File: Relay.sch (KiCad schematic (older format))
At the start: 0 parts

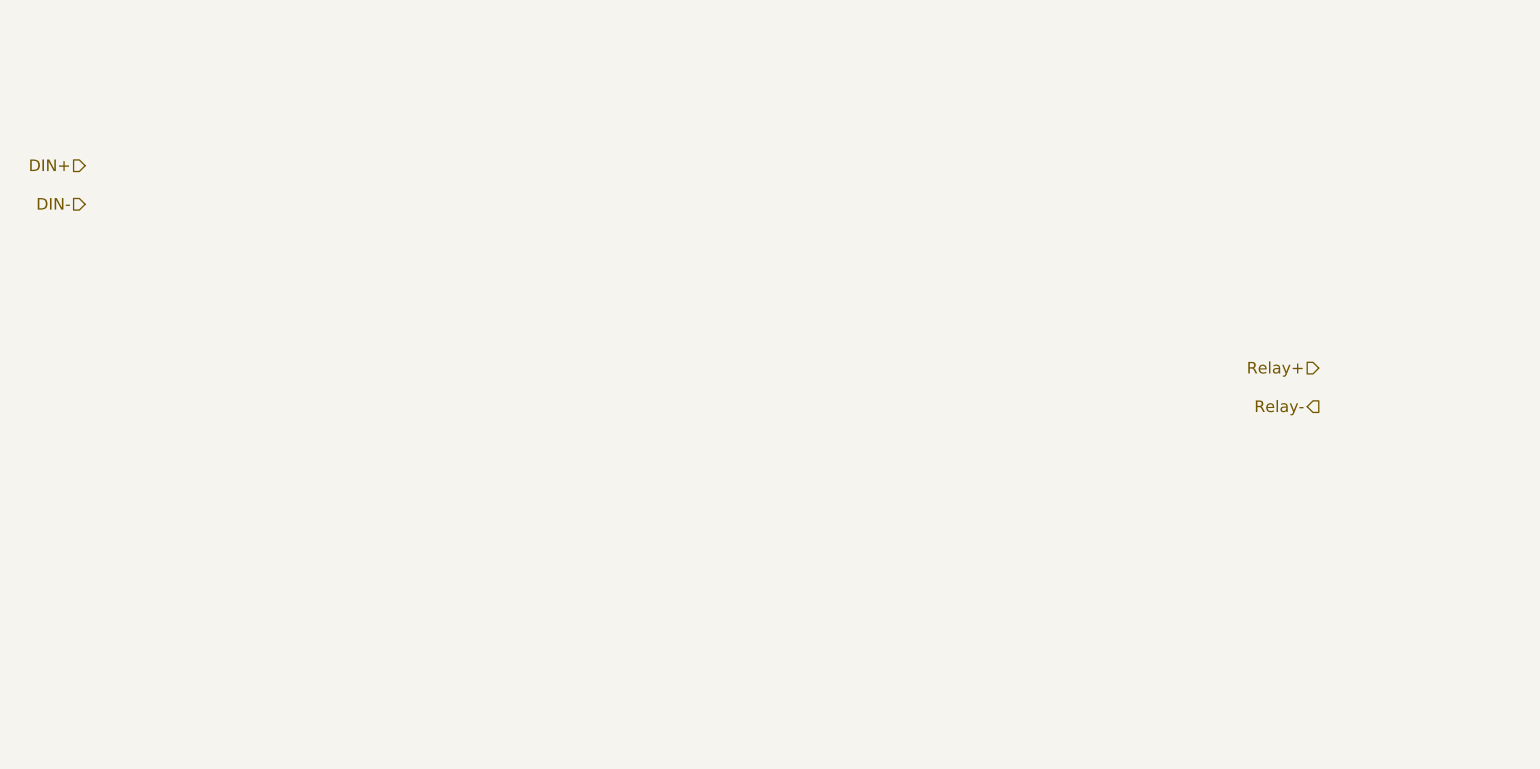
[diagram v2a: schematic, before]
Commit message: Added Relay Module Schematic
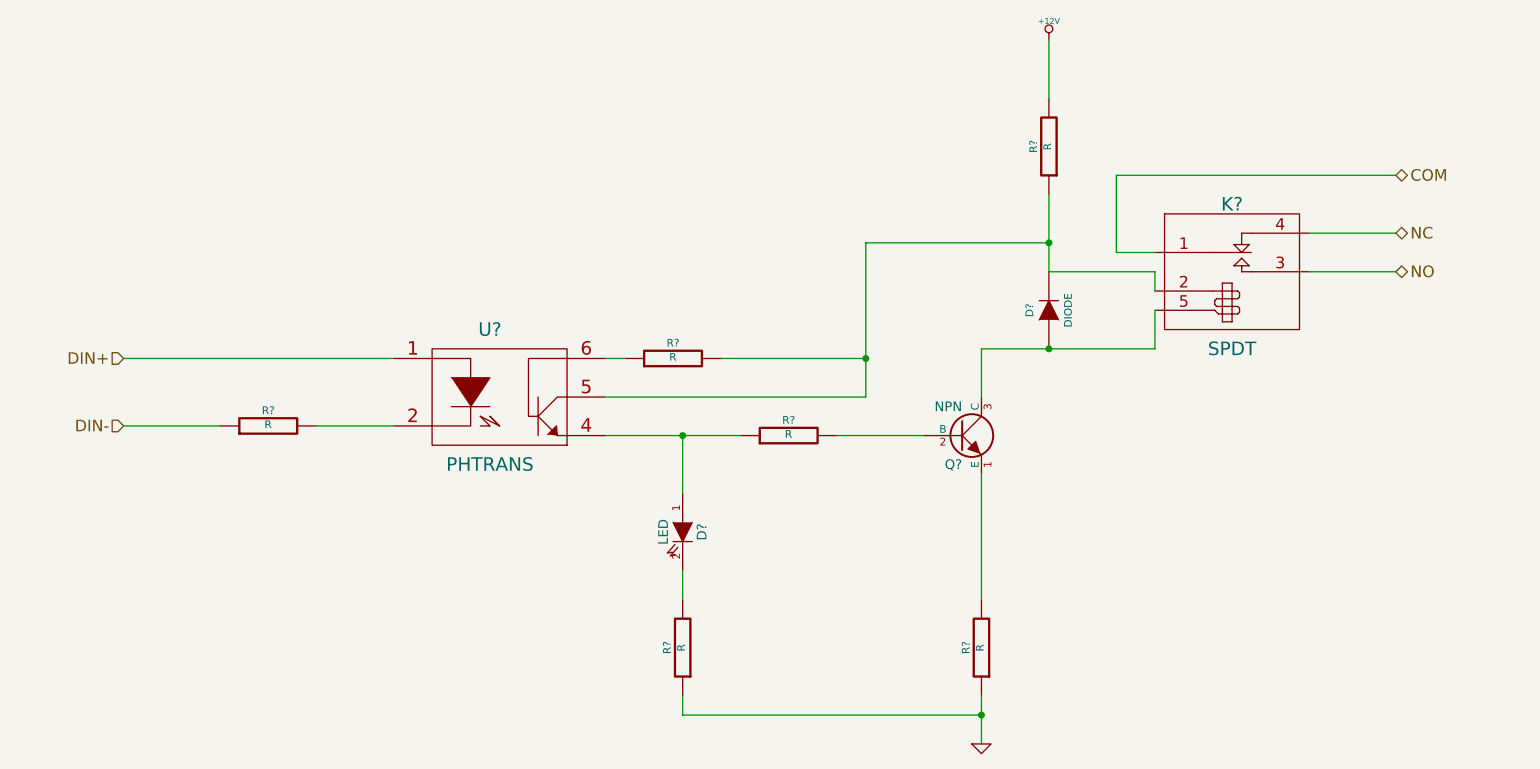
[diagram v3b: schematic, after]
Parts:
- added D?: LED, ~, symbol LED
- added D?: DIODE, ~, symbol DIODE
- added K?: SPDT, ~, symbol SPDT
- added Q?: NPN, ~, symbol NPN
- added R? (x6): R, ~, symbol R
- added U?: PHTRANS, ~, symbol PHTRANS
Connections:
- net DIN+: now also U?.1
- net DIN-: now also R?.1
- new net: R?.2, U?.2
- new net: D?.1 (A), R?.1, U?.4
- new net: D?.2 (K), K?.2 (COIL+), R?.1, R?.2, U?.5
- new net: R?.1, U?.6
- new net: Q?.2 (B), R?.2
- new net: Q?.1 (E), R?.2
- new net: D?.1 (A), K?.5 (COIL-), Q?.3 (C)
- new net: D?.2 (K), R?.2
- new net +12V: R?.2
- new net COM: K?.1 (COM)
- new net GND: R?.1, R?.1
- new net NC: K?.4 (NC)
- new net NO: K?.3 (NO)
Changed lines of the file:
@@
 LIBS:contrib
 LIBS:valves
+LIBS:BenchBuddy
 LIBS:MyBenchBuddy-cache
 EELAYER 27 0
@@
 Sheet 4 8
 Title ""
-Date "17 sep 2013"
+Date "23 sep 2013"
 Rev ""
 Comp ""
@@
 Comment4 ""
 $EndDescr
-Text HLabel 2650 2350 0    60   Input ~ 0
+Text HLabel 2850 3350 0    60   Input ~ 0
 DIN+
-Text HLabel 2650 2550 0    60   Input ~ 0
+Text HLabel 2850 3700 0    60   Input ~ 0
 DIN-
-Text HLabel 9050 3400 0    60   Input ~ 0
-Relay+
-Text HLabel 9050 3600 0    60   Output ~ 0
-Relay-
+Text HLabel 9450 2700 2    60   BiDi ~ 0
+NC
+Text HLabel 9450 2900 2    60   BiDi ~ 0
+NO
+$Comp
+L PHTRANS U?
+U 1 1 523F7A68
+P 4800 3550
+F 0 "U?" H 4750 3900 70  0000 C CNN
+F 1 "PHTRANS" H 4750 3200 70  0000 C CNN
+F 2 "~" H 4800 3550 60  0000 C CNN
+F 3 "~" H 4800 3550 60  0000 C CNN
+	1    4800 3550
+	1    0    0    -1
+$EndComp
+$Comp
+L R R?
+U 1 1 523F7A86
+P 6300 3750
+F 0 "R?" V 6380 3750 40  0000 C CNN
+F 1 "R" V 6307 3751 40  0000 C CNN
+F 2 "~" V 6230 3750 30  0000 C CNN
+F 3 "~" H 6300 3750 30  0000 C CNN
+	1    6300 3750
+	0    -1   -1   0
+$EndComp
+$Comp
+L NPN Q?
+U 1 1 523F7A95
+P 7200 3750
+F 0 "Q?" H 7200 3600 50  0000 R CNN
+F 1 "NPN" H 7200 3900 50  0000 R CNN
+F 2 "~" H 7200 3750 60  0000 C CNN
+F 3 "~" H 7200 3750 60  0000 C CNN
+	1    7200 3750
+	1    0    0    -1
+$EndComp
+$Comp
+L LED D?
+U 1 1 523F7AA4
+P 5750 4250
+F 0 "D?" H 5750 4350 50  0000 C CNN
+F 1 "LED" H 5750 4150 50  0000 C CNN
+F 2 "~" H 5750 4250 60  0000 C CNN
+F 3 "~" H 5750 4250 60  0000 C CNN
+	1    5750 4250
+	0    1    1    0
+$EndComp
+$Comp
+L SPDT K?
+U 1 1 523F8086
+P 8600 2750
+F 0 "K?" H 8600 2950 70  0000 C CNN
+F 1 "SPDT" H 8600 2200 70  0000 C CNN
+F 2 "~" H 8600 2750 60  0000 C CNN
+F 3 "~" H 8600 2750 60  0000 C CNN
+	1    8600 2750
+	1    0    0    -1
+$EndComp
+Text HLabel 9450 2400 2    60   BiDi ~ 0
+COM
+Wire Wire Line
+	9450 2700 9000 2700
+Wire Wire Line
+	9450 2900 9000 2900
+Wire Wire Line
+	9450 2400 8000 2400
+Wire Wire Line
+	8000 2400 8000 2800
+Wire Wire Line
+	8000 2800 8200 2800
+Wire Wire Line
+	5350 3750 5750 3750
+Wire Wire Line
+	5750 3750 6050 3750
+Wire Wire Line
+	6550 3750 7000 3750
+Wire Wire Line
+	7300 3950 7300 4600
+$Comp
+L R R?
+U 1 1 523F82F3
+P 7300 4850
+F 0 "R?" V 7380 4850 40  0000 C CNN
+F 1 "R" V 7307 4851 40  0000 C CNN
+F 2 "~" V 7230 4850 30  0000 C CNN
+F 3 "~" H 7300 4850 30  0000 C CNN
+	1    7300 4850
+	-1   0    0    1
+$EndComp
+$Comp
+L GND #PWR?
+U 1 1 523F8315
+P 7300 5350
+F 0 "#PWR?" H 7300 5350 30  0001 C CNN
+F 1 "GND" H 7300 5280 30  0001 C CNN
+F 2 "" H 7300 5350 60  0000 C CNN
+F 3 "" H 7300 5350 60  0000 C CNN
+	1    7300 5350
+	1    0    0    -1
+$EndComp
+Wire Wire Line
+	7300 5100 7300 5200
+Wire Wire Line
+	7300 5200 7300 5350
+Wire Wire Line
+	5750 3750 5750 4050
+Connection ~ 5750 3750
+$Comp
+L R R?
+U 1 1 523F836F
+P 5750 4850
+F 0 "R?" V 5830 4850 40  0000 C CNN
+F 1 "R" V 5757 4851 40  0000 C CNN
+F 2 "~" V 5680 4850 30  0000 C CNN
+F 3 "~" H 5750 4850 30  0000 C CNN
+	1    5750 4850
+	-1   0    0    1
+$EndComp
+Wire Wire Line
+	5750 4450 5750 4600
+Wire Wire Line
+	5750 5100 5750 5200
+Wire Wire Line
+	5750 5200 7300 5200
+Connection ~ 7300 5200
+$Comp
+L R R?
+U 1 1 523F839D
+P 7650 2250
+F 0 "R?" V 7730 2250 40  0000 C CNN
+F 1 "R" V 7657 2251 40  0000 C CNN
+F 2 "~" V 7580 2250 30  0000 C CNN
+F 3 "~" H 7650 2250 30  0000 C CNN
+	1    7650 2250
+	-1   0    0    1
+$EndComp
+$Comp
+L +12V #PWR?
+U 1 1 523F83D1
+P 7650 1700
+F 0 "#PWR?" H 7650 1650 20  0001 C CNN
+F 1 "+12V" H 7650 1800 30  0000 C CNN
+F 2 "" H 7650 1700 60  0000 C CNN
+F 3 "" H 7650 1700 60  0000 C CNN
+	1    7650 1700
+	1    0    0    -1
+$EndComp
+Wire Wire Line
+	7650 2000 7650 1700
+Wire Wire Line
+	5350 3550 6700 3550
+Wire Wire Line
+	6700 3550 6700 3350
+$Comp
+L R R?
+U 1 1 523F8436
+P 5700 3350
+F 0 "R?" V 5780 3350 40  0000 C CNN
+F 1 "R" V 5707 3351 40  0000 C CNN
+F 2 "~" V 5630 3350 30  0000 C CNN
+F 3 "~" H 5700 3350 30  0000 C CNN
+	1    5700 3350
+	0    -1   -1   0
+$EndComp
+Wire Wire Line
+	5350 3350 5450 3350
+Wire Wire Line
+	5950 3350 6700 3350
+Wire Wire Line
+	6700 3350 6700 3350
+$Comp
+L R R?
+U 1 1 523F846F
+P 3600 3700
+F 0 "R?" V 3680 3700 40  0000 C CNN
+F 1 "R" V 3607 3701 40  0000 C CNN
+F 2 "~" V 3530 3700 30  0000 C CNN
+F 3 "~" H 3600 3700 30  0000 C CNN
+	1    3600 3700
+	0    -1   -1   0
+$EndComp
+Wire Wire Line
+	3850 3700 4250 3700
+Wire Wire Line
+	2850 3700 3350 3700
+Wire Wire Line
+	2850 3350 4250 3350
+$Comp
+L DIODE D?
+U 1 1 523F8522
+P 7650 3100
+F 0 "D?" H 7650 3200 40  0000 C CNN
+F 1 "DIODE" H 7650 3000 40  0000 C CNN
+F 2 "~" H 7650 3100 60  0000 C CNN
+F 3 "~" H 7650 3100 60  0000 C CNN
+	1    7650 3100
+	0    -1   -1   0
+$EndComp
+Wire Wire Line
+	7300 3550 7300 3300
+Wire Wire Line
+	7300 3300 7650 3300
+Wire Wire Line
+	7650 3300 8200 3300
+Wire Wire Line
+	8200 3300 8200 3100
+Connection ~ 7650 3300
+Wire Wire Line
+	8200 3000 8200 2900
+Wire Wire Line
+	8200 2900 7650 2900
+Wire Wire Line
+	7650 2900 7650 2750
+Wire Wire Line
+	7650 2750 7650 2500
+Wire Wire Line
+	6700 3350 6700 2750
+Wire Wire Line
+	6700 2750 7650 2750
+Connection ~ 7650 2750
+Connection ~ 6700 3350
 $EndSCHEMATC

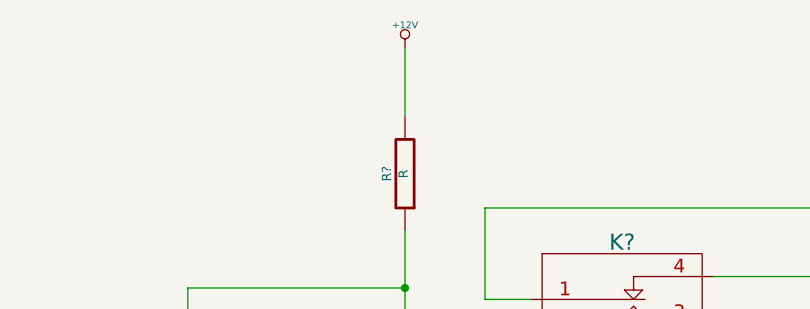
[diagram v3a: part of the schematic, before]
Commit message: Added Power Protection And Filtering Schematic
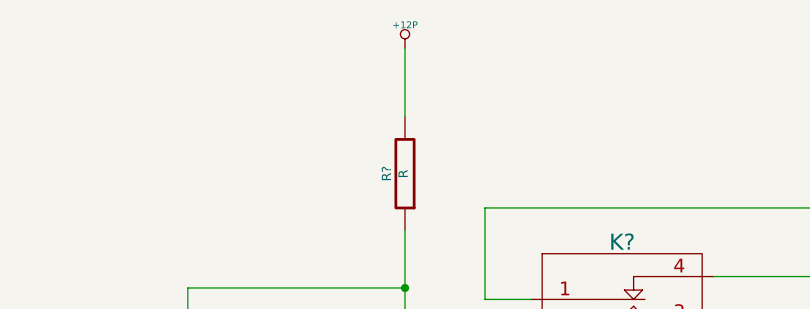
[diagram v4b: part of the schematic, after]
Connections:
- net +12V renamed +12P
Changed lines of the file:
@@
 $Descr A4 11693 8268
 encoding utf-8
-Sheet 4 8
+Sheet 4 9
 Title ""
 Date "23 sep 2013"
@@
 	-1   0    0    1
 $EndComp
-$Comp
-L +12V #PWR?
-U 1 1 523F83D1
-P 7650 1700
-F 0 "#PWR?" H 7650 1650 20  0001 C CNN
-F 1 "+12V" H 7650 1800 30  0000 C CNN
-F 2 "" H 7650 1700 60  0000 C CNN
-F 3 "" H 7650 1700 60  0000 C CNN
-	1    7650 1700
-	1    0    0    -1
-$EndComp
 Wire Wire Line
 	7650 2000 7650 1700
@@
 Connection ~ 7650 2750
 Connection ~ 6700 3350
+$Comp
+L +12P #PWR?
+U 1 1 523FADE6
+P 7650 1700
+F 0 "#PWR?" H 7650 1670 30  0001 C CNN
+F 1 "+12P" H 7650 1800 30  0000 C CNN
+F 2 "" H 7650 1700 60  0000 C CNN
+F 3 "" H 7650 1700 60  0000 C CNN
+	1    7650 1700
+	1    0    0    -1
+$EndComp
 $EndSCHEMATC

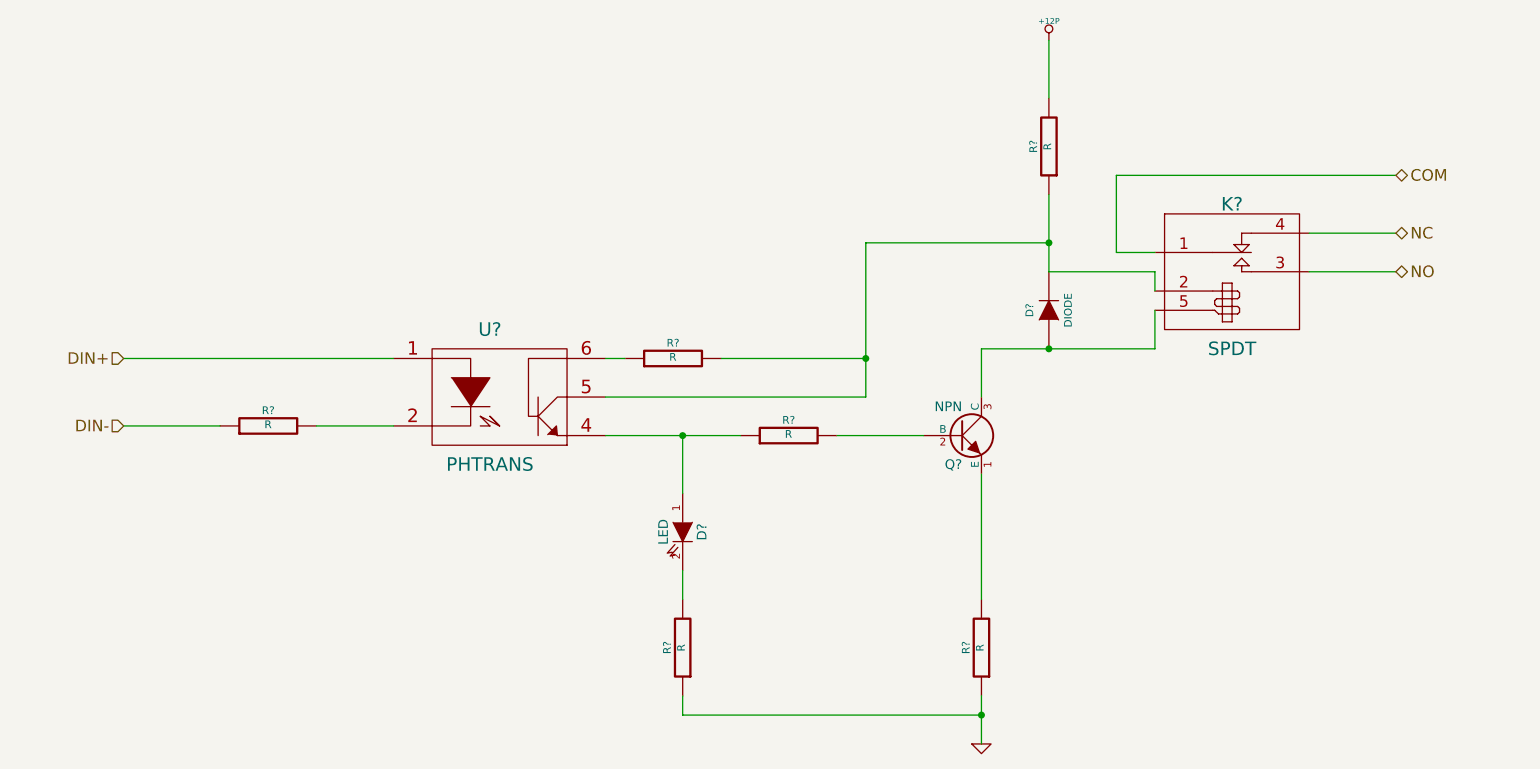
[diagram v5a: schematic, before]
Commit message: Added Arduino Block
Added Arduino Block and connected the top level of the schematic.
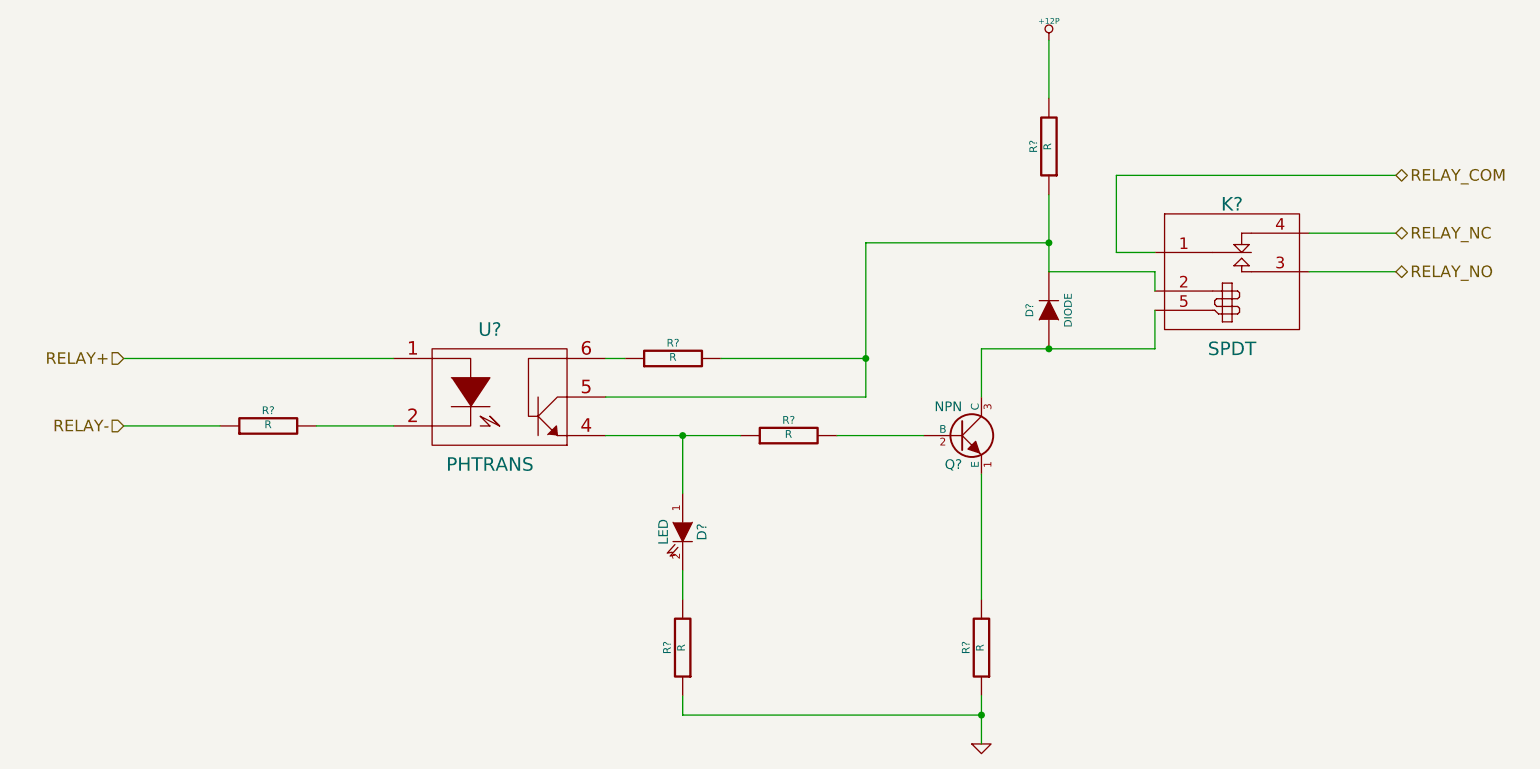
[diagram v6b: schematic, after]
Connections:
- net COM renamed RELAY_COM
- net DIN+ renamed RELAY+
- net DIN- renamed RELAY-
- net NC renamed RELAY_NC
- net NO renamed RELAY_NO
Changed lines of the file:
@@
 $EndDescr
 Text HLabel 2850 3350 0    60   Input ~ 0
-DIN+
+RELAY+
 Text HLabel 2850 3700 0    60   Input ~ 0
-DIN-
+RELAY-
 Text HLabel 9450 2700 2    60   BiDi ~ 0
-NC
+RELAY_NC
 Text HLabel 9450 2900 2    60   BiDi ~ 0
-NO
+RELAY_NO
 $Comp
 L PHTRANS U?
@@
 $EndComp
 Text HLabel 9450 2400 2    60   BiDi ~ 0
-COM
+RELAY_COM
 Wire Wire Line
 	9450 2700 9000 2700
